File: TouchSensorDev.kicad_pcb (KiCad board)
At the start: 2 copper layers, 10 parts, among them J1 Touch, J2 PINS, U1 TTP223-BA6

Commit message: finished board
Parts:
- removed the C2 at (38.9, 24.7)
- removed C3: 0.1u, Capacitor_SMD:C_1206_3216Metric_Pad1.42x1.75mm_HandSolder
- added C1: 0.1u, Capacitor_SMD:C_1206_3216Metric_Pad1.42x1.75mm_HandSolder, F.Cu at (61.5, 53.5)
- added J2: Touch, TouchSensorDev:TouchPadB, F.Cu at (82.0, 33.5)
- added J3: Touch, TouchSensorDev:TouchPadFinger, F.Cu at (57.0, 33.5)
- added JP1: Internal Pad 1, Jumper:SolderJumper-2_P1.3mm_Open_RoundedPad1.0x1.5mm, F.Cu at (41.5, 46.0)
- added JP4: TOG, Jumper:SolderJumper-2_P1.3mm_Open_RoundedPad1.0x1.5mm, F.Cu at (68.5, 54.0)
- added REF**: KiCad-Logo2_5mm_SilkScreen, Symbol:KiCad-Logo2_5mm_SilkScreen, B.Cu at (38.5, 54.5)
- added Ref**: Val**, logos:josef_adamcik_20mm_cu_mask, B.Cu at (82.5, 56.0)
- J1: footprint TestPoint:TestPoint_Pad_D4.0mm -> TouchSensorDev:TouchPadA
- JP2: value InternalPad -> Internal Pad 2; footprint Jumper:SolderJumper-2_P1.3mm_Bridged_RoundedPad1.0x1.5mm -> Jumper:SolderJumper-2_P1.3mm_Open_RoundedPad1.0x1.5mm
- JP3: value TOG -> Internal Pad 3
- U1: footprint Package_TO_SOT_SMD:SOT-23-6 -> Package_TO_SOT_SMD:SOT-23-6_Handsoldering
- moved J4 36.6 mm to (23.5, 56.6), turned to 180 degrees
- moved U1 32.3 mm to (57.5, 53.5), turned to 270 degrees
- moved JP6 31.2 mm to (74.0, 54.0), turned to 270 degrees
- moved JP2 29.0 mm to (73.5, 46.0)
- moved C2 25.1 mm to (51.5, 53.5), turned to 270 degrees
- moved JP5 24.1 mm to (29.0, 51.5)
- moved J1 21.1 mm to (32.5, 33.5)
- moved JP3 19.6 mm to (51.5, 46.0), turned to 180 degrees
- renumbered C1 to C2, J2 to J4, JP1 to JP5, JP4 to JP6
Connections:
- net Net-(J2-Pad2) renamed /OUT
- net Net-(J2-Pad3) renamed /EXTPAD
- net Net-(JP4-Pad1) renamed /AHLB
- C2 pad 1: Net-(C1-Pad1) -> /IN
- JP2 pad 1: Net-(C1-Pad1) -> /IN
- JP2 pad 2: Net-(J1-Pad1) -> Net-(J2-Pad1)
- JP3 pad 1: +5V -> /IN
- JP3 pad 2: Net-(JP3-Pad2) -> Net-(J3-Pad1)
- JP5 pad 2: Net-(C1-Pad1) -> /IN
- U1 pad 3: Net-(C1-Pad1) -> /IN
- U1 pad 6: Net-(JP3-Pad2) -> /TOG
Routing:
- net /IN: track 0.00 -> 68.4 mm
- net +5V: track 0.00 -> 54.4 mm
- net /OUT: track 0.00 -> 38.4 mm, vias 0 -> 1
- net GND: track 0.00 -> 22.1 mm, vias 0 -> 5
- net /AHLB: track 0.00 -> 20.9 mm, vias 0 -> 2
- net Net-(J2-Pad1): track 0.00 -> 16.8 mm
- net Net-(J1-Pad1): track 0.00 -> 16.0 mm, vias 0 -> 1
- net Net-(J3-Pad1): track 0.00 -> 15.0 mm
- net /TOG: track 0.00 -> 12.8 mm, vias 0 -> 2
- net /EXTPAD: track 0.00 -> 4.87 mm
- added copper zone on F.Cu, net GND
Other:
- board outline added: 75 x 40 mm
- board text added: "@josefadamcik"
- board text added: "TTP223 dev board"
- board text added: "https://josef-adamcik.cz"
- board text added: "rev. 1"

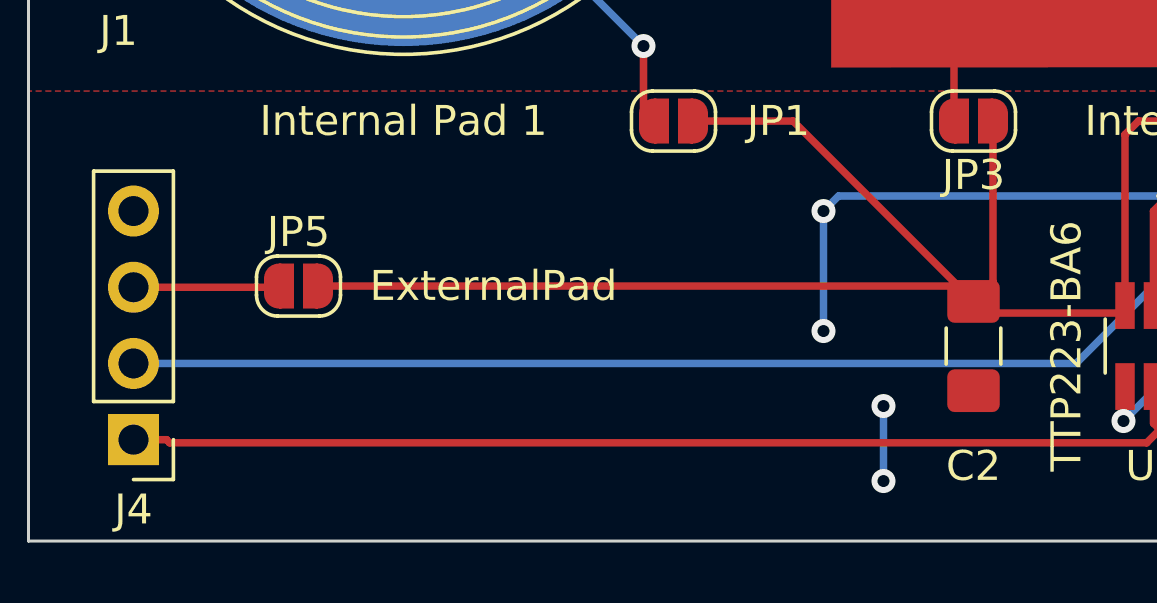
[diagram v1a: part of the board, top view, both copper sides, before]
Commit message: add labels to pin header
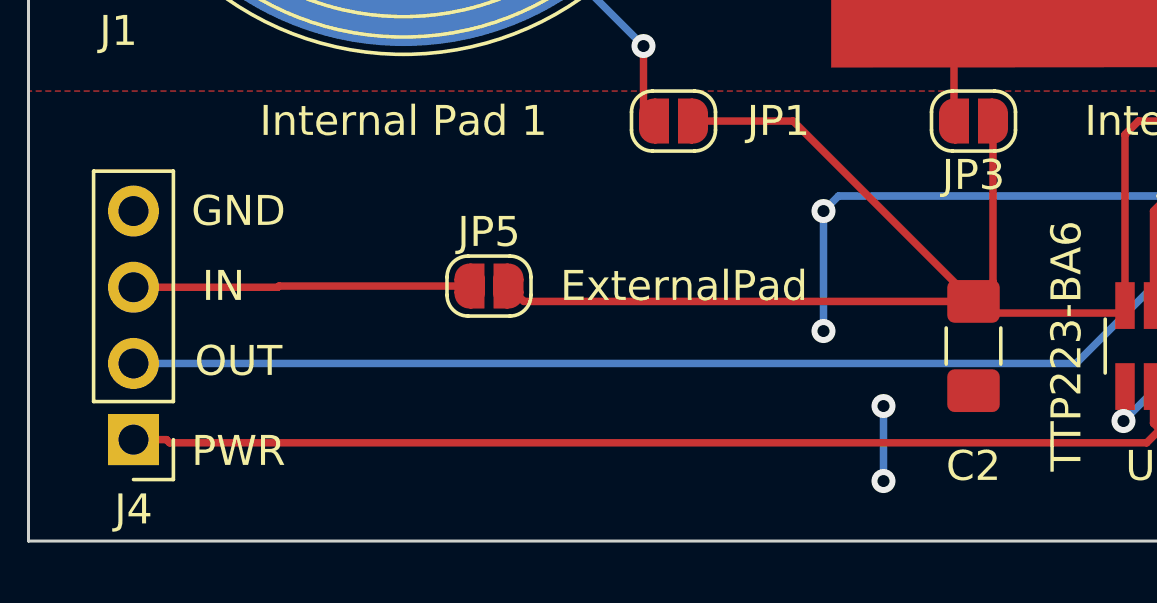
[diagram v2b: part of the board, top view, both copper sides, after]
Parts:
- moved JP5 6.35 mm to (35.4, 51.5)
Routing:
- net /EXTPAD: track 4.87 -> 11.2 mm
- net /IN: track 68.4 -> 62.8 mm
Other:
- board text added: "GND"
- board text added: "IN"
- board text added: "OUT"
- board text added: "PWR"
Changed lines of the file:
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@@
   (general
     (thickness 1.6)
-    (drawings 8)
-    (tracks 75)
+    (drawings 12)
+    (tracks 77)
     (zones 0)
     (modules 15)
@@
   )
   (module Jumper:SolderJumper-2_P1.3mm_Open_RoundedPad1.0x1.5mm (layer F.Cu)
-    (at 29 51.5)
+    (at 35.35 51.5)
     (descr "SMD Solder Jumper, 1x1.5mm, rounded Pads, 0.3mm gap, open")
     (tags "solder jumper open")
@@
       (rotate (xyz 0 0 0))
     )
+  )
+  (gr_text IN (at 26.5 51.5) (layer F.SilkS)
+    (effects (font (size 1 1) (thickness 0.15)))
+  )
+  (gr_text OUT (at 27 54) (layer F.SilkS)
+    (effects (font (size 1 1) (thickness 0.15)))
+  )
+  (gr_text PWR (at 27 57) (layer F.SilkS)
+    (effects (font (size 1 1) (thickness 0.15)))
+  )
+  (gr_text GND (at 27 49) (layer F.SilkS)
+    (effects (font (size 1 1) (thickness 0.15)))
   )
   (gr_text @josefadamcik (at 64 58) (layer B.SilkS)
@@
   (segment (start 56.55 51.62) (end 56.55 52.4) (width 0.25) (layer F.Cu) (net 6) (status 30))
   (segment (start 50.9875 51.5) (end 51.5 52.0125) (width 0.25) (layer F.Cu) (net 6) (status 30))
-  (segment (start 29.65 51.5) (end 50.9875 51.5) (width 0.25) (layer F.Cu) (net 6) (status 30))
   (segment (start 45.4875 46) (end 51.5 52.0125) (width 0.25) (layer F.Cu) (net 6) (status 20))
   (segment (start 42.15 46) (end 45.4875 46) (width 0.25) (layer F.Cu) (net 6) (status 10))
@@
   (segment (start 57 46) (end 62 46) (width 0.25) (layer F.Cu) (net 6))
   (segment (start 62 46) (end 61.926998 46) (width 0.25) (layer F.Cu) (net 6))
+  (segment (start 36.5125 52.0125) (end 36 51.5) (width 0.25) (layer F.Cu) (net 6))
+  (segment (start 51.5 52.0125) (end 36.5125 52.0125) (width 0.25) (layer F.Cu) (net 6))
   (via (at 58.5 50.5) (size 0.8) (drill 0.4) (layers F.Cu B.Cu) (net 7))
   (segment (start 54.92 54.08) (end 23.5 54.08) (width 0.25) (layer B.Cu) (net 7) (status 20))
@@
   (segment (start 58.5 52.35) (end 58.45 52.4) (width 0.25) (layer F.Cu) (net 7) (status 30))
   (segment (start 58.5 50.5) (end 58.5 52.35) (width 0.25) (layer F.Cu) (net 7) (status 20))
-  (segment (start 28.31 51.54) (end 28.35 51.5) (width 0.25) (layer F.Cu) (net 8) (status 30))
   (segment (start 23.5 51.54) (end 28.31 51.54) (width 0.25) (layer F.Cu) (net 8) (status 30))
+  (segment (start 28.35 51.5) (end 28.31 51.54) (width 0.25) (layer F.Cu) (net 8))
+  (segment (start 34.7 51.5) (end 28.35 51.5) (width 0.25) (layer F.Cu) (net 8))
   (via (at 66.5 53) (size 0.8) (drill 0.4) (layers F.Cu B.Cu) (net 9))
   (via (at 58.5 56) (size 0.8) (drill 0.4) (layers F.Cu B.Cu) (net 9))
